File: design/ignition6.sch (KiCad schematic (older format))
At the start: 8 parts, among them P6 CONN_1, P7 CONN_1, Q1 RFP30N06

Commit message: updating bom, lets commit this before I run a script to update the footprints for the resistors
Signed-off-by: Jared Harvey <TortiseGIT@jaredharvey.com>
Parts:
- D17: footprint LEDV -> LED-0805
- D76: footprint (none) -> SOD-123
- P6, P7: footprint 1PIN -> PINTST
- Q1: footprint TO220_sm -> TO220_VERT
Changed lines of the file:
@@
-EESchema Schematic File Version 2  date 2/14/2011 7:45:18 AM
+EESchema Schematic File Version 2  date 2/16/2011 5:39:16 AM
 LIBS:power
 LIBS:freeEMS_lib
@@
 EELAYER END
 $Descr A4 11700 8267
-Sheet 39 55
+Sheet 39 56
 Title "Puma board"
-Date "14 feb 2011"
+Date "16 feb 2011"
 Rev "v0.02"
 Comp "diyefi.org"
@@
 F 0 "D76" H 4300 2150 40  0000 C CNN
 F 1 "DIODE" H 4300 1950 40  0000 C CNN
+F 2 "SOD-123" H 4300 2050 60  0001 C CNN
 F 4 "Micro Commercial Co" V 1130 2600 60  0001 C CNN "mfg"
 F 5 "1N4148W-TP" V 1130 2600 60  0001 C CNN "mfg#"
@@
 F 0 "Q1" H 4010 2220 60  0000 R CNN
 F 1 "RFP30N06" H 4010 1900 60  0000 R CNN
-F 2 "TO220_sm" V 3930 2800 60  0001 C CNN
+F 2 "TO220_VERT" V 3930 2800 60  0001 C CNN
 F 4 "Fairchild Semi" V 1130 2600 60  0001 C CNN "mfg"
 F 5 "RFP30N06LE" V 1130 2600 60  0001 C CNN "mfg#"
@@
 F 0 "D17" H 3850 1750 50  0000 C CNN
 F 1 "LED" H 3850 1550 50  0000 C CNN
-F 2 "LEDV" V 1680 5050 60  0001 C CNN
+F 2 "LED-0805" V 1680 5050 60  0001 C CNN
 F 4 "OSRAM" V 1130 2600 60  0001 C CNN "mfg"
 F 5 "LH R974-LP-1-0-20-R18" V 1130 2600 60  0001 C CNN "mfg#"
@@
 F 0 "P7" H 4480 1750 40  0000 L CNN
 F 1 "CONN_1" H 4400 1805 30  0001 C CNN
-F 2 "1PIN" V 830 1950 60  0001 C CNN
+F 2 "PINTST" V 830 1950 60  0001 C CNN
 	1    4400 1750
 	1    0    0    -1
@@
 F 0 "P6" H 4480 1450 40  0000 L CNN
 F 1 "CONN_1" H 4400 1505 30  0001 C CNN
-F 2 "1PIN" V 830 1850 60  0001 C CNN
+F 2 "PINTST" V 830 1850 60  0001 C CNN
 	1    4400 1450
 	1    0    0    -1

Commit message: Schematic BOM is now fully populated with only 3 exceptions, .cmp file is obsolete at this point, so it has been removed.
Signed-off-by: Jared Harvey <TortiseGIT@jaredharvey.com>
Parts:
- R15, R17, R18: footprint R4-SM0805 -> SM0805
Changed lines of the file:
@@
-EESchema Schematic File Version 2  date 2/16/2011 5:39:16 AM
+EESchema Schematic File Version 2  date 2/16/2011 8:44:20 AM
 LIBS:power
 LIBS:freeEMS_lib
@@
 F 0 "R18" V 3480 2300 50  0000 C CNN
 F 1 "10k" V 3400 2300 50  0000 C CNN
-F 2 "R4-SM0805" V 3580 2400 60  0001 C CNN
+F 2 "SM0805" V 1130 2600 60  0001 C CNN
 F 4 "Stackpole" V 1130 2600 60  0001 C CNN "mfg"
 F 5 "RMCF0805JT10K0CT" V 1130 2600 60  0001 C CNN "mfg#"
@@
 F 0 "R17" V 3380 1650 50  0000 C CNN
 F 1 "3.3k" V 3300 1650 50  0000 C CNN
-F 2 "R4-SM0805" V 1980 1650 60  0001 C CNN
+F 2 "SM0805" V 1130 2600 60  0001 C CNN
 F 4 "Stackpole" V 1130 2600 60  0001 C CNN "mfg"
 F 5 "RMCF0805JT3K30CT" V 1130 2600 60  0001 C CNN "mfg#"
@@
 F 0 "R15" V 3180 2050 50  0000 C CNN
 F 1 "1k" V 3100 2050 50  0000 C CNN
-F 2 "R4-SM0805" V 3280 2150 60  0001 C CNN
+F 2 "SM0805" V 1130 2600 60  0001 C CNN
 F 4 "Stackpole" V 1130 2600 60  0001 C CNN "mfg"
 F 5 "RMCF0805JT1K00" V 1130 2600 60  0001 C CNN "mfg#"

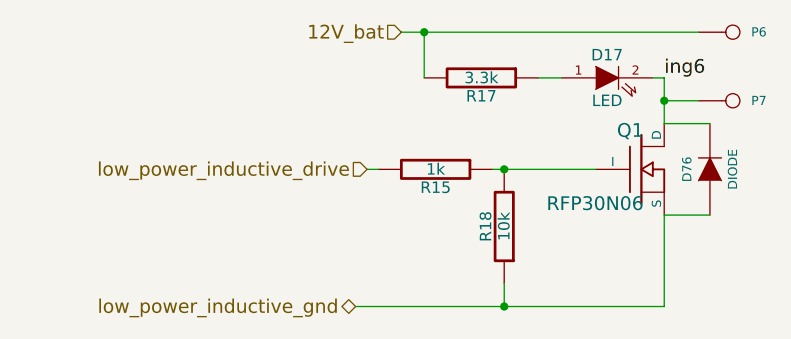
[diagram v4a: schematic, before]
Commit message: Silkscreen rearrange, fat 12v track ready to be removed, VR resistors changed to 1210, intra-protection circuits removed, changed XOR resistor to 330ohm, new config for FT232, fixed osc schematic, fixed MAP diagnosis pullup
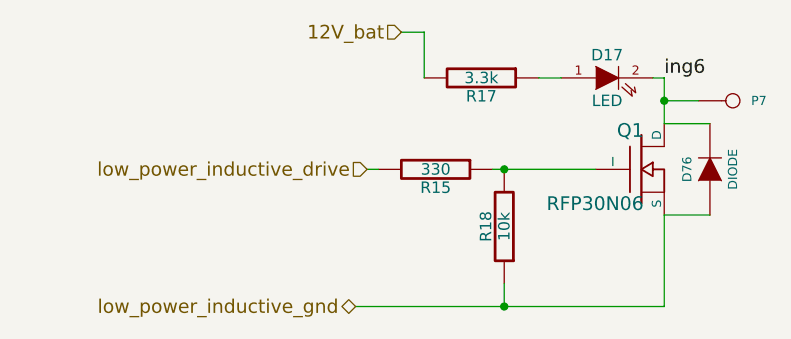
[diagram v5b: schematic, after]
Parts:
- removed P6: CONN_1, PINTST, symbol CONN_1
- R15: value 1k -> 330
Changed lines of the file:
@@
-EESchema Schematic File Version 2  date 2/20/2011 12:36:47 PM
+EESchema Schematic File Version 2  date Wed 23 Feb 2011 05:11:09 AM ART
 LIBS:power
 LIBS:freeEMS_lib
@@
 EELAYER END
 $Descr A4 11700 8267
-Sheet 39 56
+Sheet 39 54
 Title "Puma board"
-Date "20 feb 2011"
+Date "23 feb 2011"
 Rev "v0.02"
 Comp "diyefi.org"
@@
 	3400 2550 3400 2650
 Wire Wire Line
-	3050 1450 3050 1650
+	3050 1650 3050 1450
 Wire Wire Line
 	4100 1650 4100 1850
 Wire Wire Line
-	4100 2250 4100 2650
+	4100 2650 4100 2250
 Wire Wire Line
 	2800 2050 2850 2050
@@
 	3350 2050 3800 2050
 Wire Wire Line
-	4100 2650 2750 2650
+	2750 2650 4100 2650
 Wire Wire Line
 	4100 1650 4050 1650
@@
 Connection ~ 3400 2050
 Wire Wire Line
-	4250 1450 2950 1450
-Connection ~ 3050 1450
+	3050 1450 2950 1450
 Wire Wire Line
 	4100 1850 4300 1850
@@
 $EndComp
 $Comp
-L CONN_1 P6
-U 1 1 4C2F5311
-P 4400 1450
-F 0 "P6" H 4480 1450 40  0000 L CNN
-F 1 "CONN_1" H 4400 1505 30  0001 C CNN
-F 2 "PINTST" V 830 1850 60  0001 C CNN
-	1    4400 1450
-	1    0    0    -1
-$EndComp
-$Comp
 L R R15
 U 1 1 4C2F52E7
 P 3100 2050
 F 0 "R15" V 3180 2050 50  0000 C CNN
-F 1 "1k" V 3100 2050 50  0000 C CNN
+F 1 "330" V 3100 2050 50  0000 C CNN
 F 2 "SM0805" V 1130 2600 60  0001 C CNN
 F 4 "Stackpole" V 1130 2600 60  0001 C CNN "mfg"

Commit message: Fixed P&H footprints
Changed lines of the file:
@@
-EESchema Schematic File Version 2  date Wed 23 Feb 2011 05:38:40 AM ART
+EESchema Schematic File Version 2  date Thu 24 Feb 2011 06:52:52 PM ART
 LIBS:power
 LIBS:freeEMS_lib
@@
 Sheet 39 54
 Title "Puma board"
-Date "23 feb 2011"
+Date "24 feb 2011"
 Rev "v0.02"
 Comp "diyefi.org"
@@
 	4100 1650 4100 1850
 Wire Wire Line
-	4100 2650 4100 2250
+	4100 2250 4100 2650
 Wire Wire Line
 	2800 2050 2850 2050
@@
 	3350 2050 3800 2050
 Wire Wire Line
-	2750 2650 4100 2650
+	4100 2650 2750 2650
 Wire Wire Line
 	4100 1650 4050 1650
